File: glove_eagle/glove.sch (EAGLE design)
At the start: 51 parts, among them J1 MICRO_USB_B_JST_MC5BR3-M404-4S, U1 BNO055, U3 NRF51822QF, U4 MCP73831, X3 ABS05-32.768KHZ-9-T

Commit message: Finished routing nearly complete board
Still lots of modifications to make, but it's a start.
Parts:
- removed R14: (no value), passives:RESISTOR0603_RES
- added C5: 8 nF, passives:CAPACITOR0603_CAP
- added C6, C7: 10 uF, passives:CAPACITOR0603_CAP
- added CN1: (no value), adafruit:JST_2PIN-SMT-RA
- added SW1: (no value), adafruit:DPDT-EG1390
- added U2: LP3855EMP-ADJ, LP3855EMP-ADJ:LP3855EMP-ADJ
- R12: value (none) -> 440
- R13: value (none) -> 250
- R15, R16, R17, R18: value (none) -> 10 k
- R9: value (none) -> 47 k
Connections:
- removed net I2C_ADDR_SEL: U1.COM3
- removed net N$10: R13.1
- removed net N$11: R14.2, U$1.KEY4
- removed net N$13: R14.1
- removed net N$6: R12.2, U$1.KEY6
- removed net N$8: R13.2, U$1.KEY5
- new net N$5: C6.2, SW11.O, SW12.O, U2.VIN
- net GND: now also C6.1, C7.2, CN1.1, R13.2, U1.COM3, U2.GND
- net N$1: now also CN1.2, SW11.P, SW12.P
- net N$7: now also C5.1, R12.2, R13.1, U2.ADJ; no longer R12.1
- net VCC: now also C5.2, C7.1, R12.1, U2.VOUT
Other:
- note added: "I2C_ADDR_SEL"
- moved on the sheet: C1, C2, C3, J1, LED1, R10, R6, R7, U4

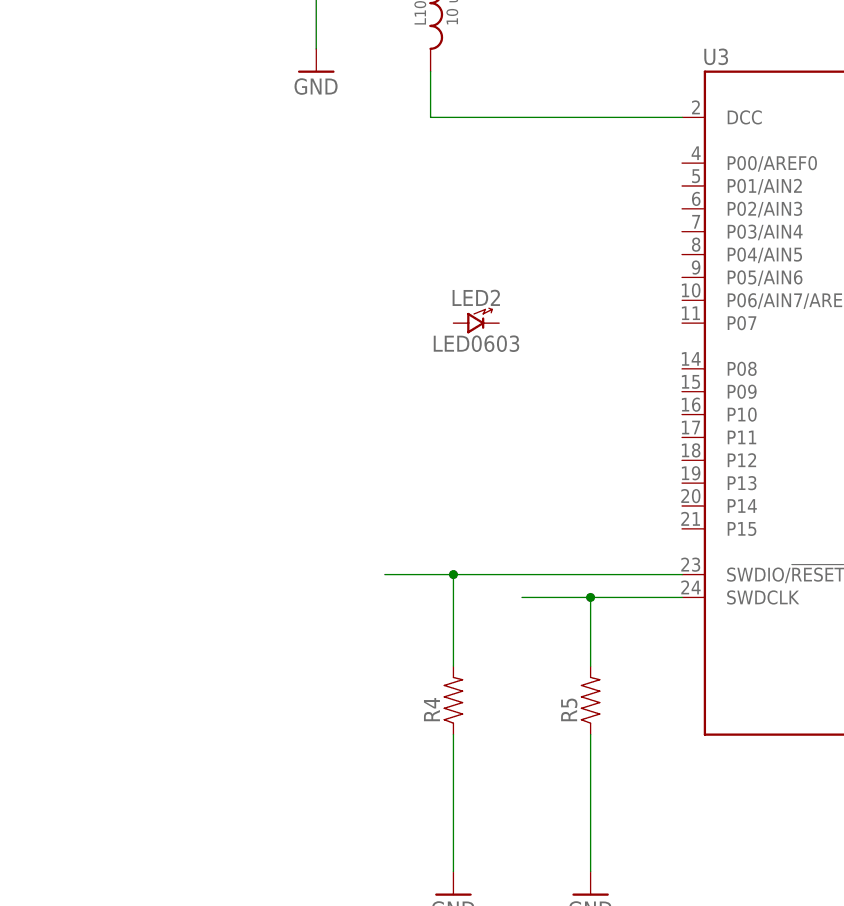
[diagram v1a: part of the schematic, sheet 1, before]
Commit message: Added traces to board for I2C
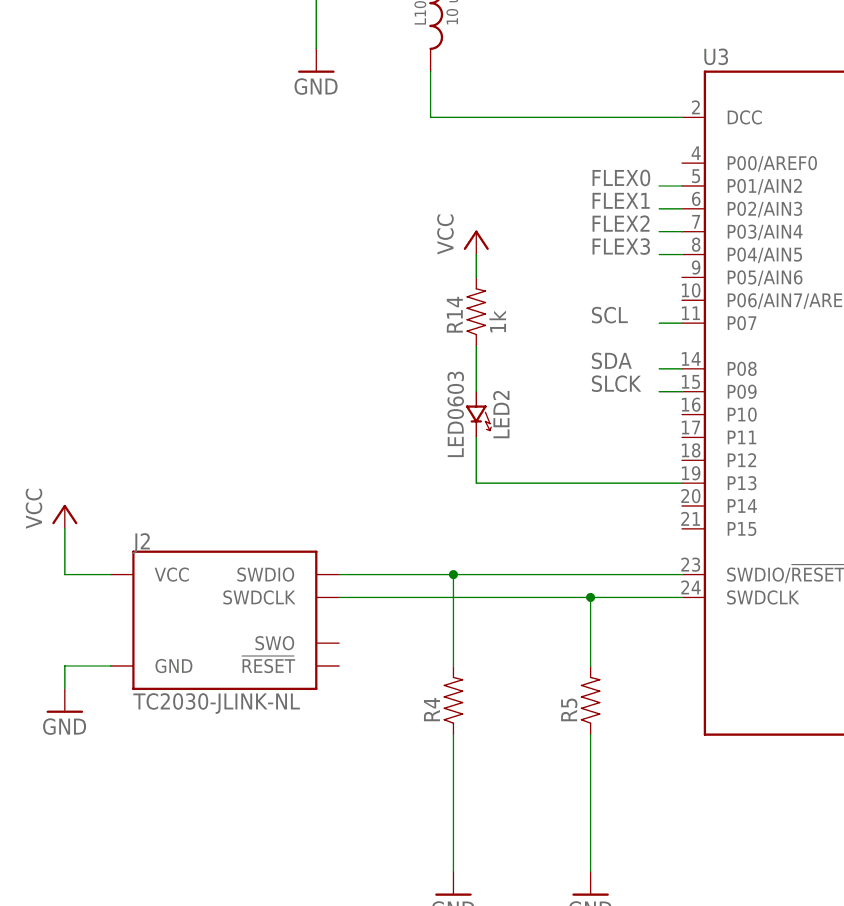
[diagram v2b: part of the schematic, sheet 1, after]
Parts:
- added J2: TC2030-JLINK-NL, connector:TC2030-JLINK-NL
- added R14: 1k, passives:RESISTOR0603_RES
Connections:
- new net FLEX0: U3.P01/AIN2
- new net FLEX1: U3.P02/AIN3
- new net FLEX2: U3.P03/AIN4
- new net FLEX3: U3.P04/AIN5
- new net N$6: LED2.CATHODE, U3.P13
- new net N$8: LED2.ANODE, R14.1
- new net SLCK: U3.P09
- net GND: now also J2.GND
- net N$19: now also J2.SWDIO
- net N$30: now also J2.SWDCLK
- net SCL: now also U3.P07
- net SDA: now also U3.P08
- net VCC: now also J2.VCC, R14.2
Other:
- moved on the sheet: LED2
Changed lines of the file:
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@@
 <?xml version="1.0" encoding="utf-8"?>
 <!DOCTYPE eagle SYSTEM "eagle.dtd">
-<eagle version="6.6.0">
+<eagle version="7.6.0">
 <drawing>
 <settings>
@@
 <part name="C7" library="passives" deviceset="CAPACITOR" device="0603_CAP" value="10 uF"/>
 <part name="GND8" library="supply1" deviceset="GND" device=""/>
+<part name="P+4" library="supply1" deviceset="VCC" device=""/>
+<part name="GND15" library="supply1" deviceset="GND" device=""/>
+<part name="J2" library="connector" deviceset="TC2030-JLINK" device="-NL"/>
+<part name="R14" library="passives" deviceset="RESISTOR" device="0603_RES" value="1k"/>
+<part name="P+5" library="supply1" deviceset="VCC" device=""/>
 </parts>
 <sheets>
@@
 <instance part="R4" gate="G$1" x="-48.26" y="-35.56" rot="R90"/>
 <instance part="R5" gate="G$1" x="-33.02" y="-35.56" rot="R90"/>
-<instance part="LED2" gate="G$1" x="-45.72" y="5.08"/>
+<instance part="LED2" gate="G$1" x="-45.72" y="-5.08" rot="R270"/>
+<instance part="P+4" gate="VCC" x="-91.44" y="-15.24"/>
+<instance part="GND15" gate="1" x="-91.44" y="-38.1"/>
+<instance part="J2" gate="G$1" x="-73.66" y="-27.94"/>
+<instance part="R14" gate="G$1" x="-45.72" y="7.62" rot="R90"/>
+<instance part="P+5" gate="VCC" x="-45.72" y="15.24"/>
 </instances>
 <busses>
@@
 <pinref part="GND14" gate="1" pin="GND"/>
 <wire x1="-48.26" y1="-40.64" x2="-48.26" y2="-55.88" width="0.1524" layer="91"/>
+</segment>
+<segment>
+<pinref part="GND15" gate="1" pin="GND"/>
+<wire x1="-86.36" y1="-33.02" x2="-91.44" y2="-33.02" width="0.1524" layer="91"/>
+<wire x1="-91.44" y1="-33.02" x2="-91.44" y2="-35.56" width="0.1524" layer="91"/>
+<pinref part="J2" gate="G$1" pin="GND"/>
 </segment>
 </net>
@@
 <junction x="-2.54" y="68.58"/>
 </segment>
+<segment>
+<pinref part="P+4" gate="VCC" pin="VCC"/>
+<wire x1="-86.36" y1="-22.86" x2="-91.44" y2="-22.86" width="0.1524" layer="91"/>
+<wire x1="-91.44" y1="-22.86" x2="-91.44" y2="-17.78" width="0.1524" layer="91"/>
+<pinref part="J2" gate="G$1" pin="VCC"/>
+</segment>
+<segment>
+<pinref part="P+5" gate="VCC" pin="VCC"/>
+<pinref part="R14" gate="G$1" pin="2"/>
+<wire x1="-45.72" y1="12.7" x2="-45.72" y2="10.16" width="0.1524" layer="91"/>
+</segment>
 </net>
 <net name="N$19" class="0">
@@
 <wire x1="-22.86" y1="-22.86" x2="-48.26" y2="-22.86" width="0.1524" layer="91"/>
 <wire x1="-48.26" y1="-22.86" x2="-48.26" y2="-33.02" width="0.1524" layer="91"/>
-<wire x1="-48.26" y1="-22.86" x2="-55.88" y2="-22.86" width="0.1524" layer="91"/>
+<wire x1="-60.96" y1="-22.86" x2="-48.26" y2="-22.86" width="0.1524" layer="91"/>
 <junction x="-48.26" y="-22.86"/>
+<pinref part="J2" gate="G$1" pin="SWDIO"/>
 </segment>
 </net>
@@
 <wire x1="-22.86" y1="-25.4" x2="-33.02" y2="-25.4" width="0.1524" layer="91"/>
 <wire x1="-33.02" y1="-25.4" x2="-33.02" y2="-33.02" width="0.1524" layer="91"/>
-<wire x1="-33.02" y1="-25.4" x2="-40.64" y2="-25.4" width="0.1524" layer="91"/>
+<wire x1="-33.02" y1="-25.4" x2="-60.96" y2="-25.4" width="0.1524" layer="91"/>
 <junction x="-33.02" y="-25.4"/>
+<pinref part="J2" gate="G$1" pin="SWDCLK"/>
+</segment>
+</net>
+<net name="SCL" class="0">
+<segment>
+<pinref part="U3" gate="G$1" pin="P07"/>
+<wire x1="-22.86" y1="5.08" x2="-25.4" y2="5.08" width="0.1524" layer="91"/>
+<label x="-33.02" y="5.08" size="1.778" layer="95"/>
+</segment>
+</net>
+<net name="SDA" class="0">
+<segment>
+<pinref part="U3" gate="G$1" pin="P08"/>
+<wire x1="-22.86" y1="0" x2="-25.4" y2="0" width="0.1524" layer="91"/>
+<label x="-33.02" y="0" size="1.778" layer="95"/>
+</segment>
+</net>
+<net name="SLCK" class="0">
+<segment>
+<pinref part="U3" gate="G$1" pin="P09"/>
+<wire x1="-22.86" y1="-2.54" x2="-25.4" y2="-2.54" width="0.1524" layer="91"/>
+<label x="-33.02" y="-2.54" size="1.778" layer="95"/>
+</segment>
+</net>
+<net name="FLEX0" class="0">
+<segment>
+<pinref part="U3" gate="G$1" pin="P01/AIN2"/>
+<wire x1="-22.86" y1="20.32" x2="-25.4" y2="20.32" width="0.1524" layer="91"/>
+<label x="-33.02" y="20.32" size="1.778" layer="95"/>
+</segment>
+</net>
+<net name="FLEX1" class="0">
+<segment>
+<pinref part="U3" gate="G$1" pin="P02/AIN3"/>
+<wire x1="-22.86" y1="17.78" x2="-25.4" y2="17.78" width="0.1524" layer="91"/>
+<label x="-33.02" y="17.78" size="1.778" layer="95"/>
+</segment>
+</net>
+<net name="FLEX2" class="0">
+<segment>
+<pinref part="U3" gate="G$1" pin="P03/AIN4"/>
+<wire x1="-22.86" y1="15.24" x2="-25.4" y2="15.24" width="0.1524" layer="91"/>
+<label x="-33.02" y="15.24" size="1.778" layer="95"/>
+</segment>
+</net>
+<net name="FLEX3" class="0">
+<segment>
+<pinref part="U3" gate="G$1" pin="P04/AIN5"/>
+<wire x1="-22.86" y1="12.7" x2="-25.4" y2="12.7" width="0.1524" layer="91"/>
+<label x="-33.02" y="12.7" size="1.778" layer="95"/>
+</segment>
+</net>
+<net name="N$6" class="0">
+<segment>
+<pinref part="LED2" gate="G$1" pin="CATHODE"/>
+<pinref part="U3" gate="G$1" pin="P13"/>
+<wire x1="-45.72" y1="-7.62" x2="-45.72" y2="-12.7" width="0.1524" layer="91"/>
+<wire x1="-45.72" y1="-12.7" x2="-22.86" y2="-12.7" width="0.1524" layer="91"/>
+</segment>
+</net>
+<net name="N$8" class="0">
+<segment>
+<pinref part="R14" gate="G$1" pin="1"/>
+<pinref part="LED2" gate="G$1" pin="ANODE"/>
+<wire x1="-45.72" y1="2.54" x2="-45.72" y2="-2.54" width="0.1524" layer="91"/>
 </segment>
 </net>
@@
 <wire x1="12.7" y1="-17.78" x2="12.7" y2="-20.32" width="0.1524" layer="91"/>
 <wire x1="12.7" y1="-20.32" x2="-5.08" y2="-20.32" width="0.1524" layer="91"/>
-<pinref part="C5" gate="G$1" pin="2"/>
-<wire x1="-5.08" y1="-20.32" x2="-5.08" y2="-17.78" width="0.1524" layer="91"/>
 <wire x1="-5.08" y1="-20.32" x2="-12.7" y2="-20.32" width="0.1524" layer="91"/>
 <junction x="-5.08" y="-20.32"/>
@@
 <wire x1="-5.08" y1="-22.86" x2="-5.08" y2="-20.32" width="0.1524" layer="91"/>
 <label x="-20.32" y="-20.32" size="1.778" layer="95"/>
-</segment>
-</net>
+<pinref part="C5" gate="G$1" pin="2"/>
+<wire x1="-5.08" y1="-17.78" x2="-5.08" y2="-20.32" width="0.1524" layer="91"/>
+</segment>
+</net>
